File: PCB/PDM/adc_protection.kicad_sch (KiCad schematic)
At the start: 24 parts

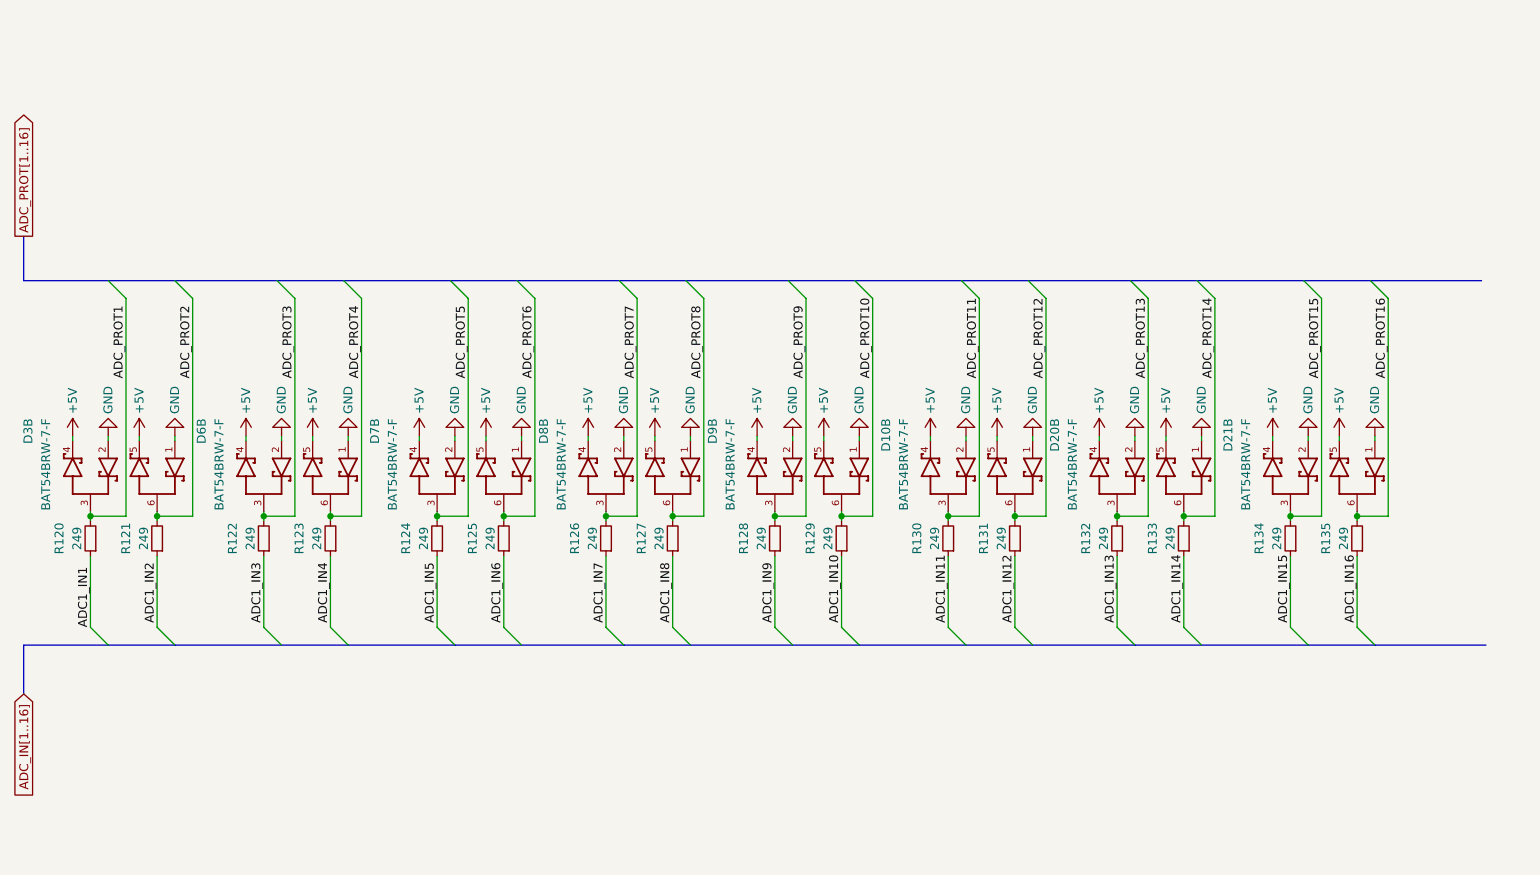
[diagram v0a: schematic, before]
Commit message: Modified ADC protection section
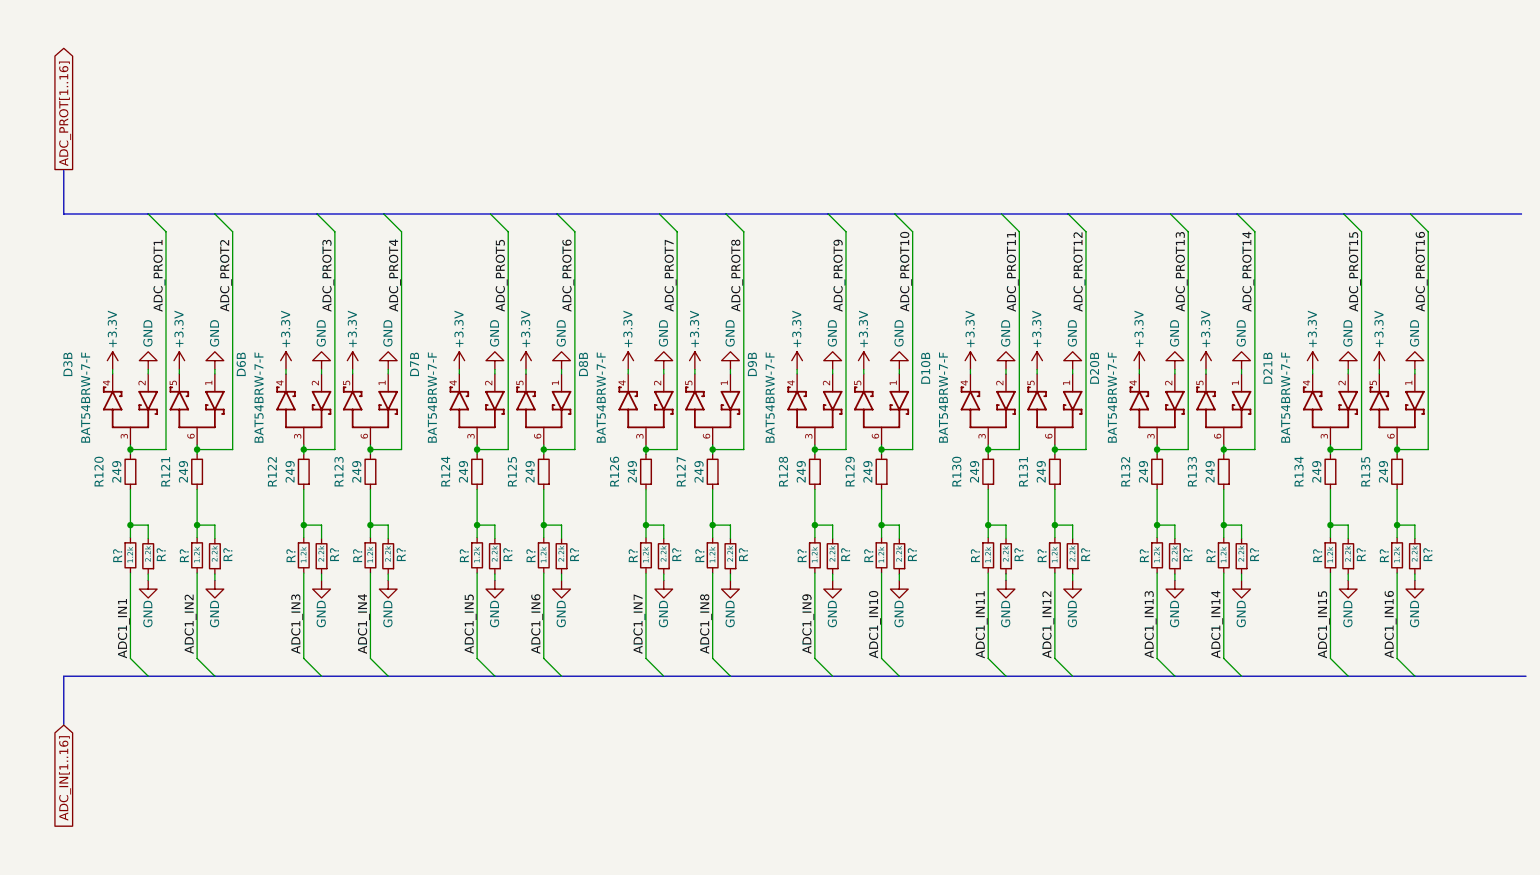
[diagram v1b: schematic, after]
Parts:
- added R? (x16): 1.2k, symbol Device:R_Small
- added R? (x16): 2.2k, symbol Device:R_Small
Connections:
- net ADC1_IN1: now also R?.2; no longer R120.1
- net ADC1_IN10: now also R?.2; no longer R129.1
- net ADC1_IN11: now also R?.2; no longer R130.1
- net ADC1_IN12: now also R?.2; no longer R131.1
- net ADC1_IN13: now also R?.2; no longer R132.1
- net ADC1_IN14: now also R?.2; no longer R133.1
- net ADC1_IN15: now also R?.2; no longer R134.1
- net ADC1_IN16: now also R?.2; no longer R135.1
- net ADC1_IN2: now also R?.2; no longer R121.1
- net ADC1_IN3: now also R?.2; no longer R122.1
- net ADC1_IN4: now also R?.2; no longer R123.1
- net ADC1_IN5: now also R?.2; no longer R124.1
- net ADC1_IN6: now also R?.2; no longer R125.1
- net ADC1_IN7: now also R?.2; no longer R126.1
- net ADC1_IN8: now also R?.2; no longer R127.1
- net ADC1_IN9: now also R?.2; no longer R128.1
- net GND: now also R?.1, R?.1, R?.1, R?.1, R?.1, R?.1, R?.1, R?.1, R?.1, R?.1, R?.1, R?.1, R?.1, R?.1, R?.1, R?.1
- net +5V renamed +3.3V
- new net: R132.1, R?.1, R?.2
- new net: R134.1, R?.1, R?.2
- new net: R124.1, R?.1, R?.2
- new net: R123.1, R?.1, R?.2
- new net: R135.1, R?.1, R?.2
- new net: R129.1, R?.1, R?.2
- new net: R125.1, R?.1, R?.2
- new net: R131.1, R?.1, R?.2
- new net: R133.1, R?.1, R?.2
- new net: R122.1, R?.1, R?.2
- new net: R126.1, R?.1, R?.2
- new net: R121.1, R?.1, R?.2
- new net: R128.1, R?.1, R?.2
- new net: R130.1, R?.1, R?.2
- new net: R127.1, R?.1, R?.2
- new net: R120.1, R?.1, R?.2
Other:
- moved on the sheet: D10B, D20B, D21B, D3B, D6B, D7B, D8B, D9B, R120, R121, R122, R123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
